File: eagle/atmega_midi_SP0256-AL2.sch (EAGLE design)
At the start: 44 parts, among them U1 6N138, U2 ATMEGA328P_PDIP, U3 SP0256-AL2, U4 TL072P

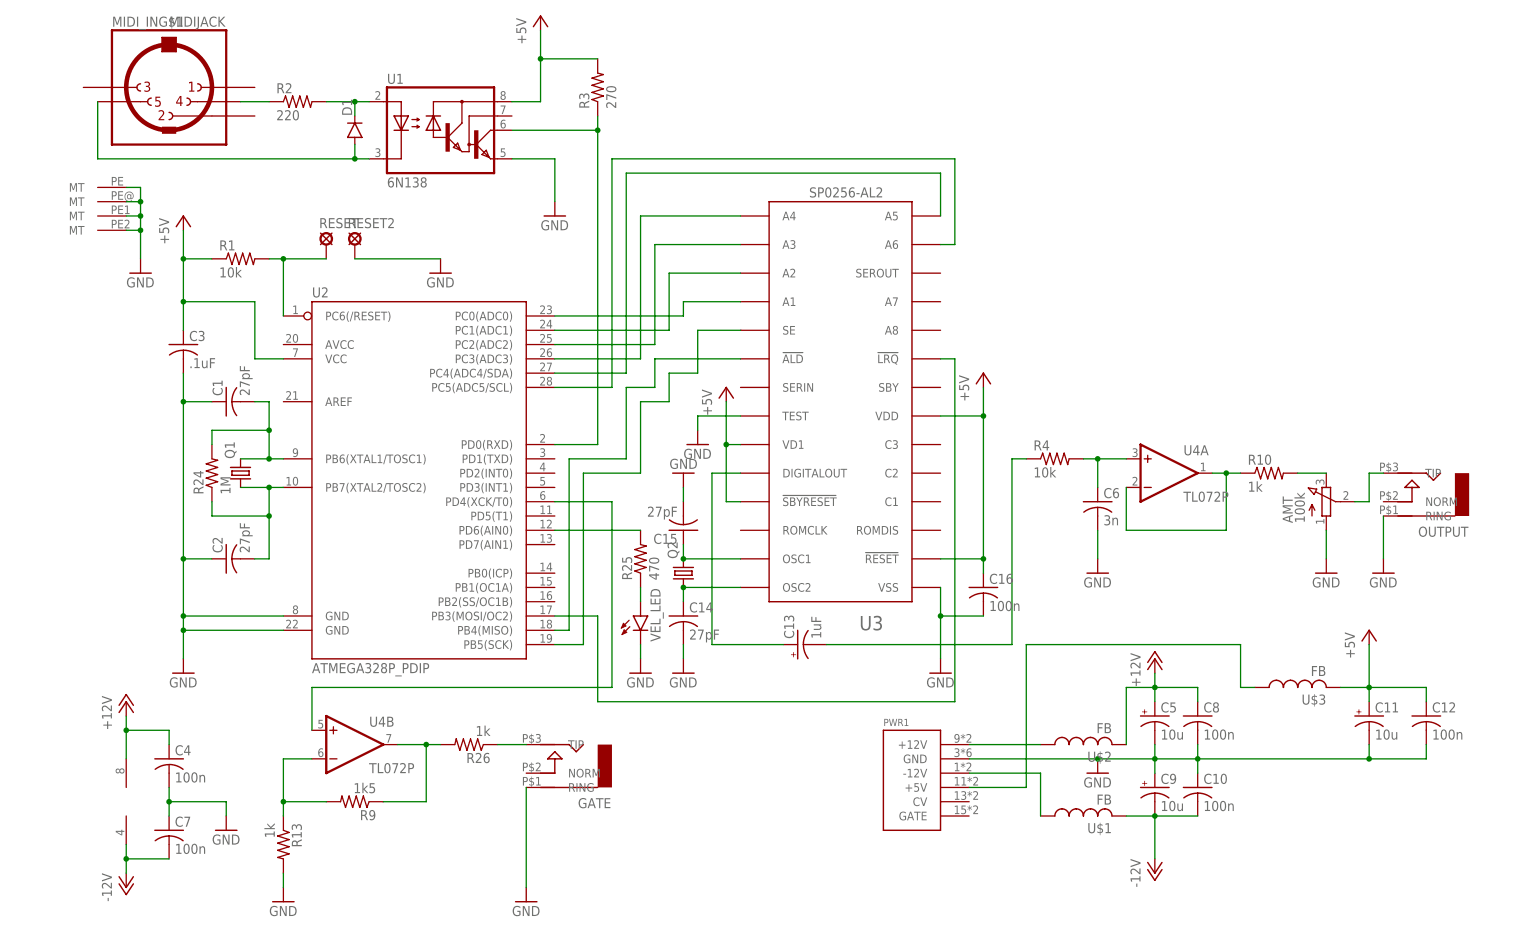
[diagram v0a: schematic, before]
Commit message: schematic corrected for reset control
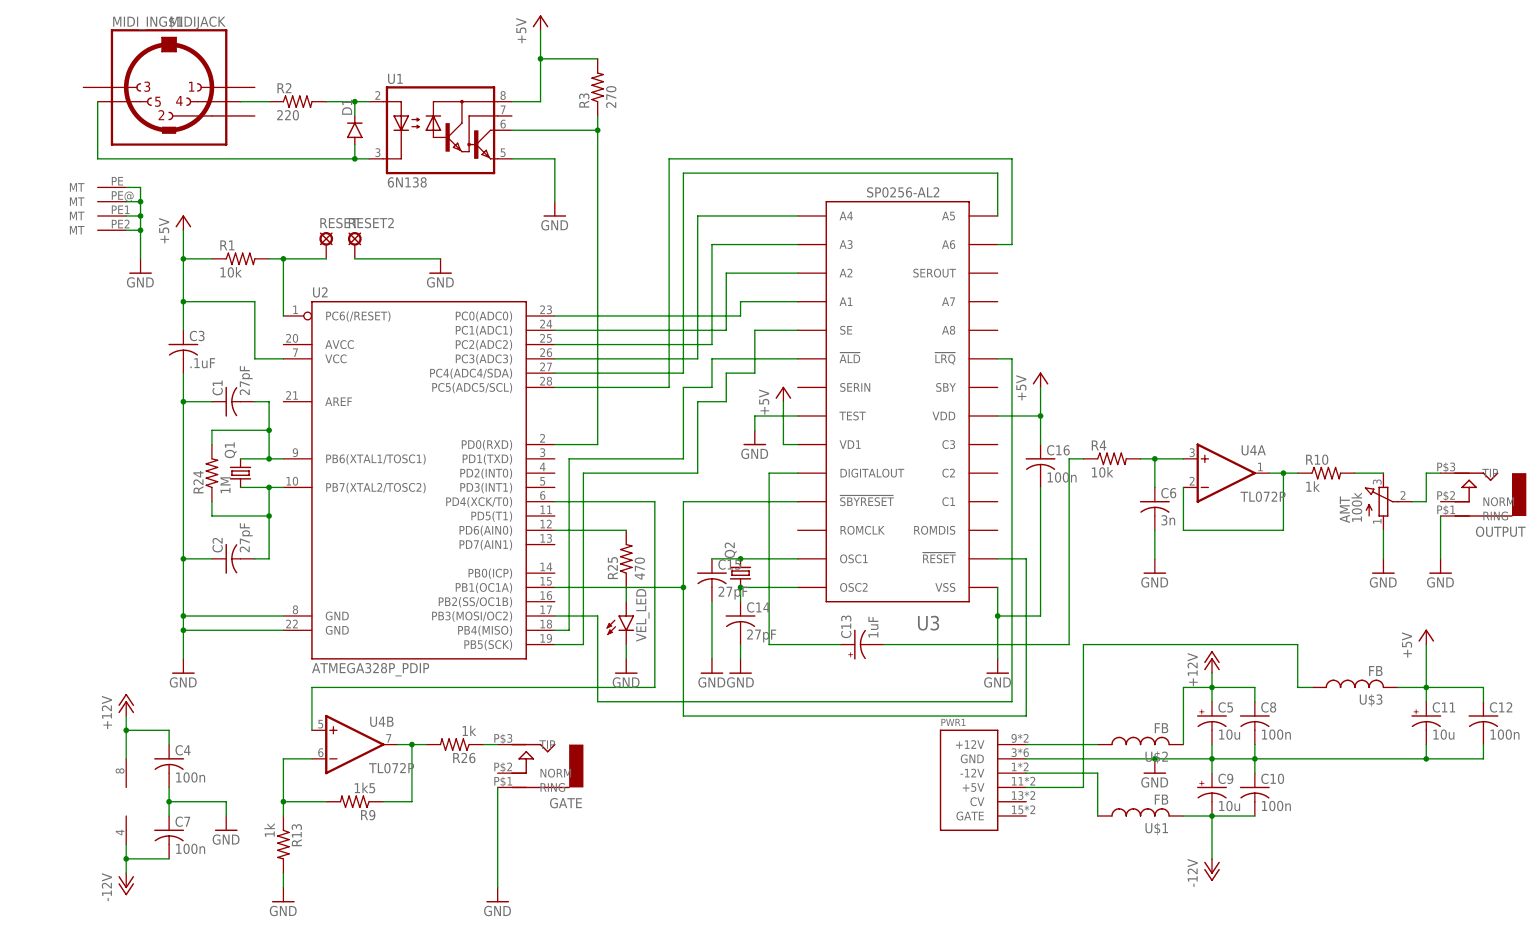
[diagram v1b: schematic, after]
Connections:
- new net N$1: U2.PB1(OC1A), U3.!RESET, U3.!SBYRESET
- net +5V: no longer U3.!RESET, U3.!SBYRESET
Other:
- moved on the sheet: AMT, C10, C11, C12, C13, C14, C15, C16, C5, C6, C8, C9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

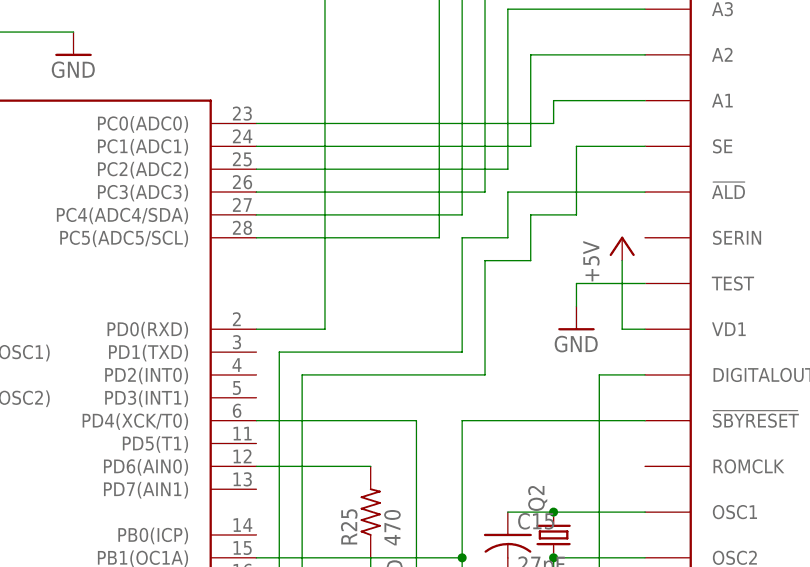
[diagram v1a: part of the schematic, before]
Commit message: board corrected for reset control
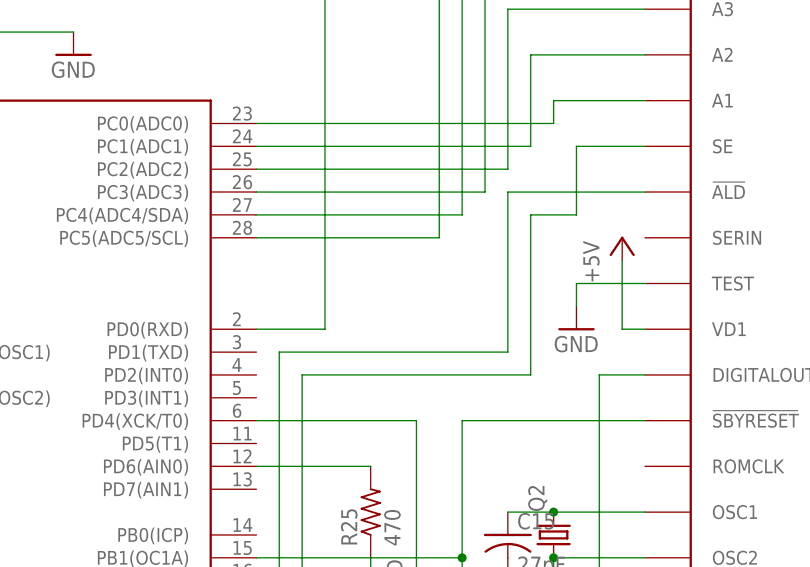
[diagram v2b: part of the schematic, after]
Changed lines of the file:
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@@
 <net name="N$15" class="0">
 <segment>
-<wire x1="68.58" y1="66.04" x2="68.58" y2="60.96" width="0.1524" layer="91"/>
-<wire x1="68.58" y1="60.96" x2="63.5" y2="60.96" width="0.1524" layer="91"/>
-<wire x1="63.5" y1="60.96" x2="63.5" y2="48.26" width="0.1524" layer="91"/>
-<wire x1="63.5" y1="48.26" x2="43.18" y2="48.26" width="0.1524" layer="91"/>
+<wire x1="68.58" y1="66.04" x2="68.58" y2="48.26" width="0.1524" layer="91"/>
+<wire x1="68.58" y1="48.26" x2="43.18" y2="48.26" width="0.1524" layer="91"/>
 <wire x1="43.18" y1="48.26" x2="43.18" y2="17.78" width="0.1524" layer="91"/>
 <pinref part="U2" gate="G$1" pin="PB4(MISO)"/>
@@
 <wire x1="40.64" y1="15.24" x2="45.72" y2="15.24" width="0.1524" layer="91"/>
 <wire x1="45.72" y1="15.24" x2="45.72" y2="45.72" width="0.1524" layer="91"/>
-<wire x1="45.72" y1="45.72" x2="66.04" y2="45.72" width="0.1524" layer="91"/>
-<wire x1="66.04" y1="45.72" x2="66.04" y2="58.42" width="0.1524" layer="91"/>
-<wire x1="66.04" y1="58.42" x2="71.12" y2="58.42" width="0.1524" layer="91"/>
-<wire x1="71.12" y1="58.42" x2="71.12" y2="63.5" width="0.1524" layer="91"/>
+<wire x1="45.72" y1="45.72" x2="71.12" y2="45.72" width="0.1524" layer="91"/>
+<wire x1="71.12" y1="45.72" x2="71.12" y2="63.5" width="0.1524" layer="91"/>
 <wire x1="71.12" y1="63.5" x2="76.2" y2="63.5" width="0.1524" layer="91"/>
 <wire x1="76.2" y1="63.5" x2="76.2" y2="71.12" width="0.1524" layer="91"/>

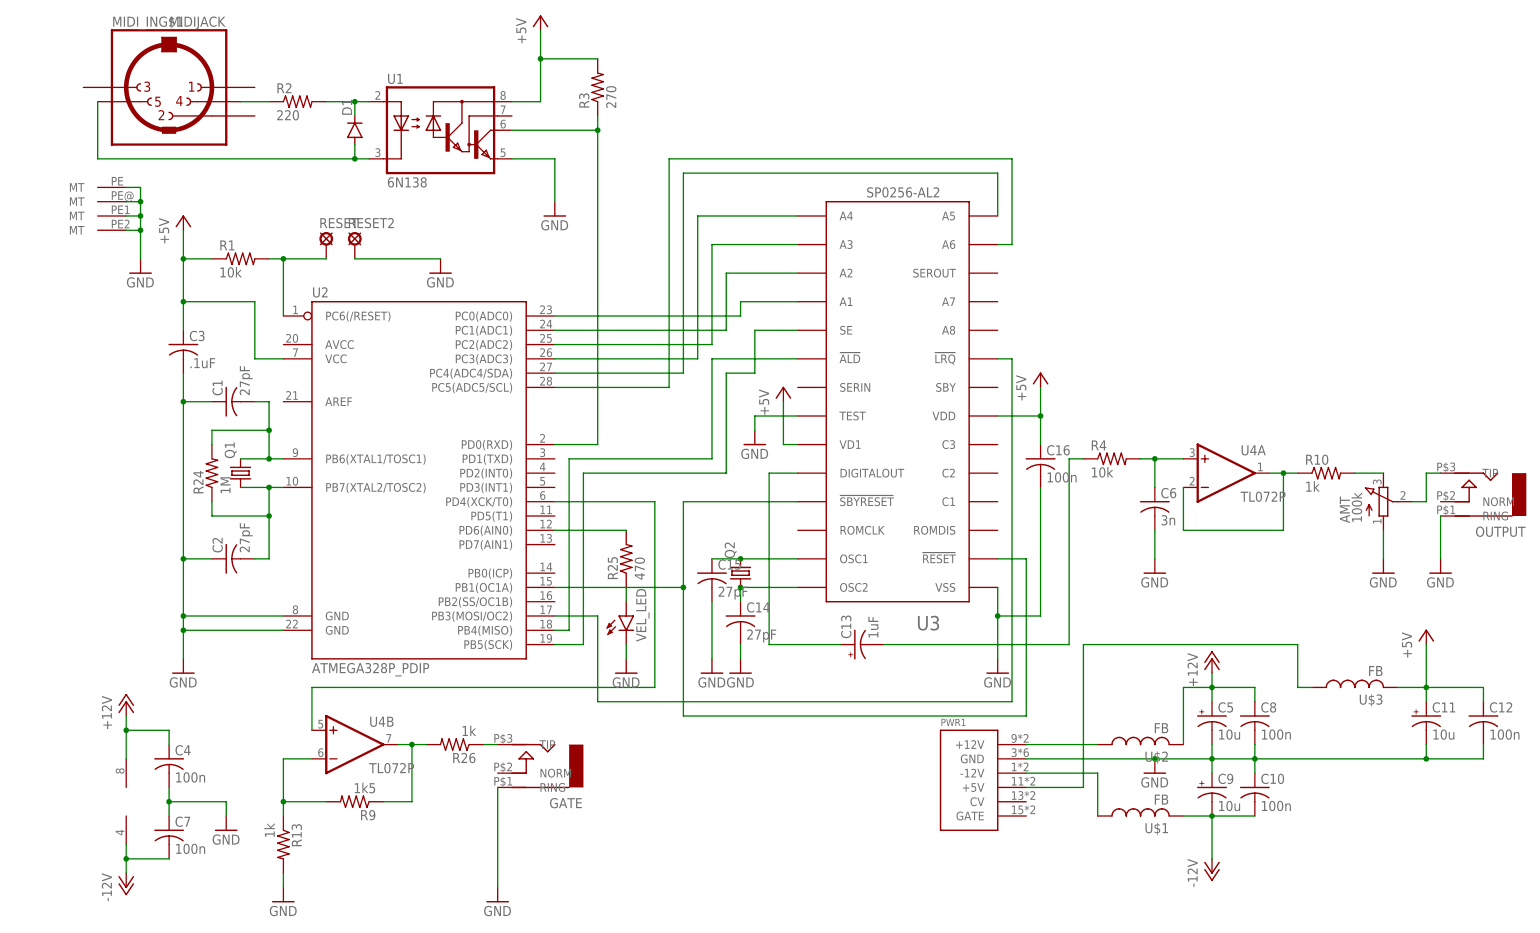
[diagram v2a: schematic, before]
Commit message: added ltc6904
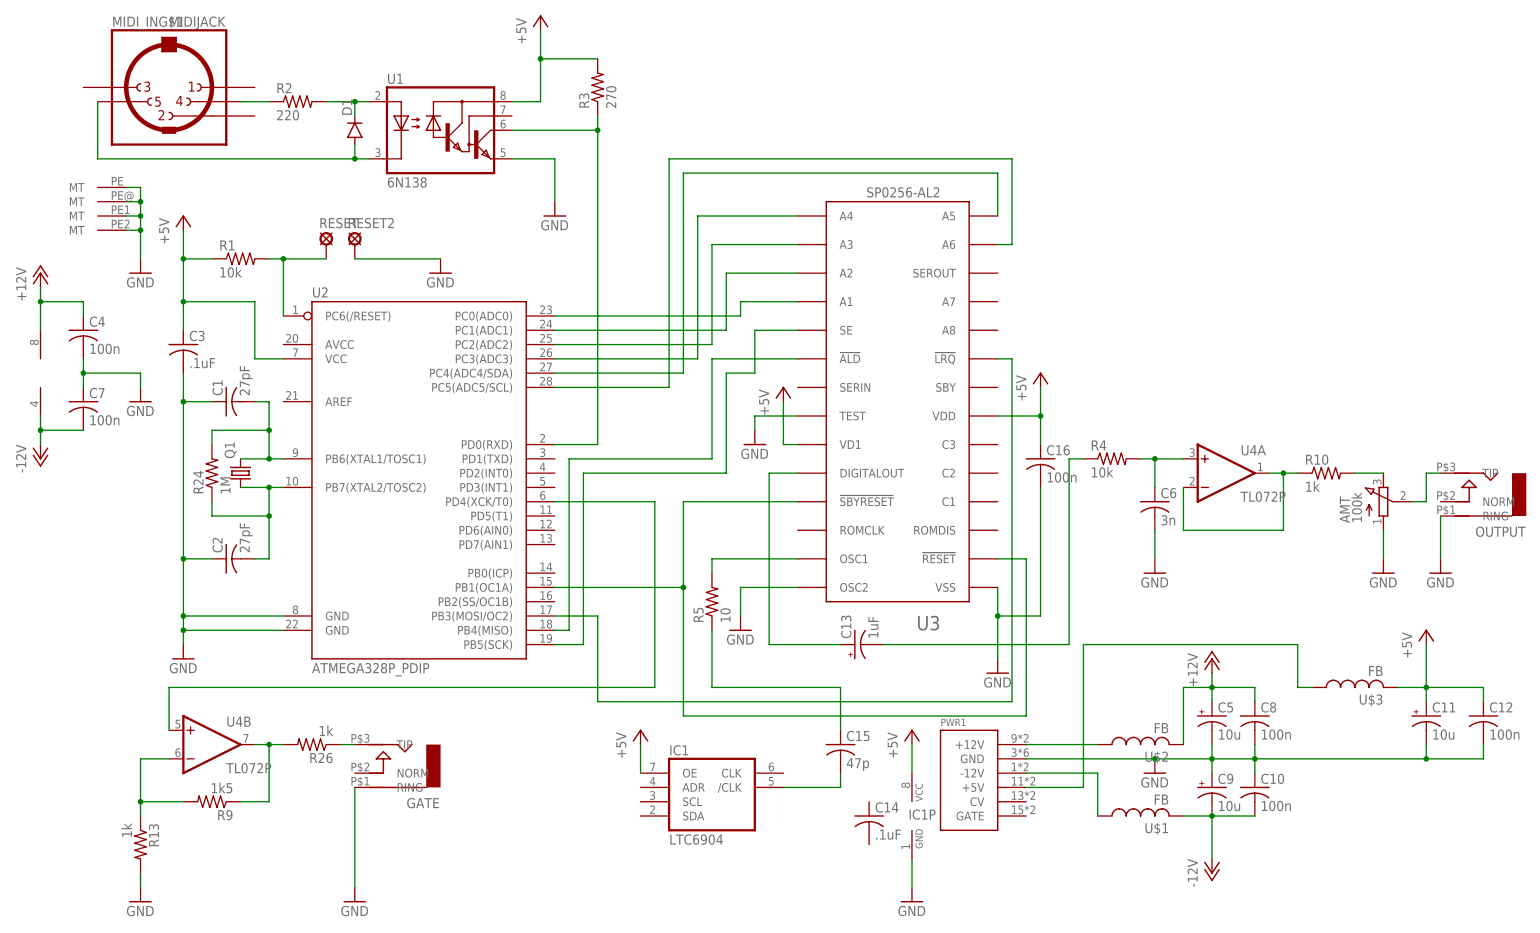
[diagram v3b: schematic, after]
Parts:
- removed Q2: (no value), crystal:CRYSTALHC49S
- removed R25: 470, rcl:R-US_0207/7
- removed VEL_LED: (no value), SparkFun-LED:LED5MM
- added IC1: LTC6904, linear-technology-3:LTC6904
- added R5: 10, rcl:R-US_0207/7
- C14: value 27pF -> .1uF; device rcl:C-US025-040X050 -> rcl:C-US025-030X050
- C15: value 27pF -> 47p; device rcl:C-US025-040X050 -> rcl:C-US050-024X044
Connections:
- removed net N$18: R25.1, VEL_LED.A
- removed net N$20: R25.2, U2.PD6(AIN0)
- removed net N$38: C14.1, Q2.1, U3.OSC2
- new net N$29: C15.2, IC1G$1./CLK
- new net N$33: R5.2, U3.OSC1
- net +5V: now also IC1G$1.OE, IC1P.VCC
- net GND: now also IC1P.GND, U3.OSC2; no longer C14.2, C15.2, VEL_LED.C
- net N$39: now also R5.1; no longer Q2.2, U3.OSC1
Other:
- moved on the sheet: C14, C15, C4, C7, GATE, R13, R26, R9, U4B

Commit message: renamed arduino code file and new board taking shape
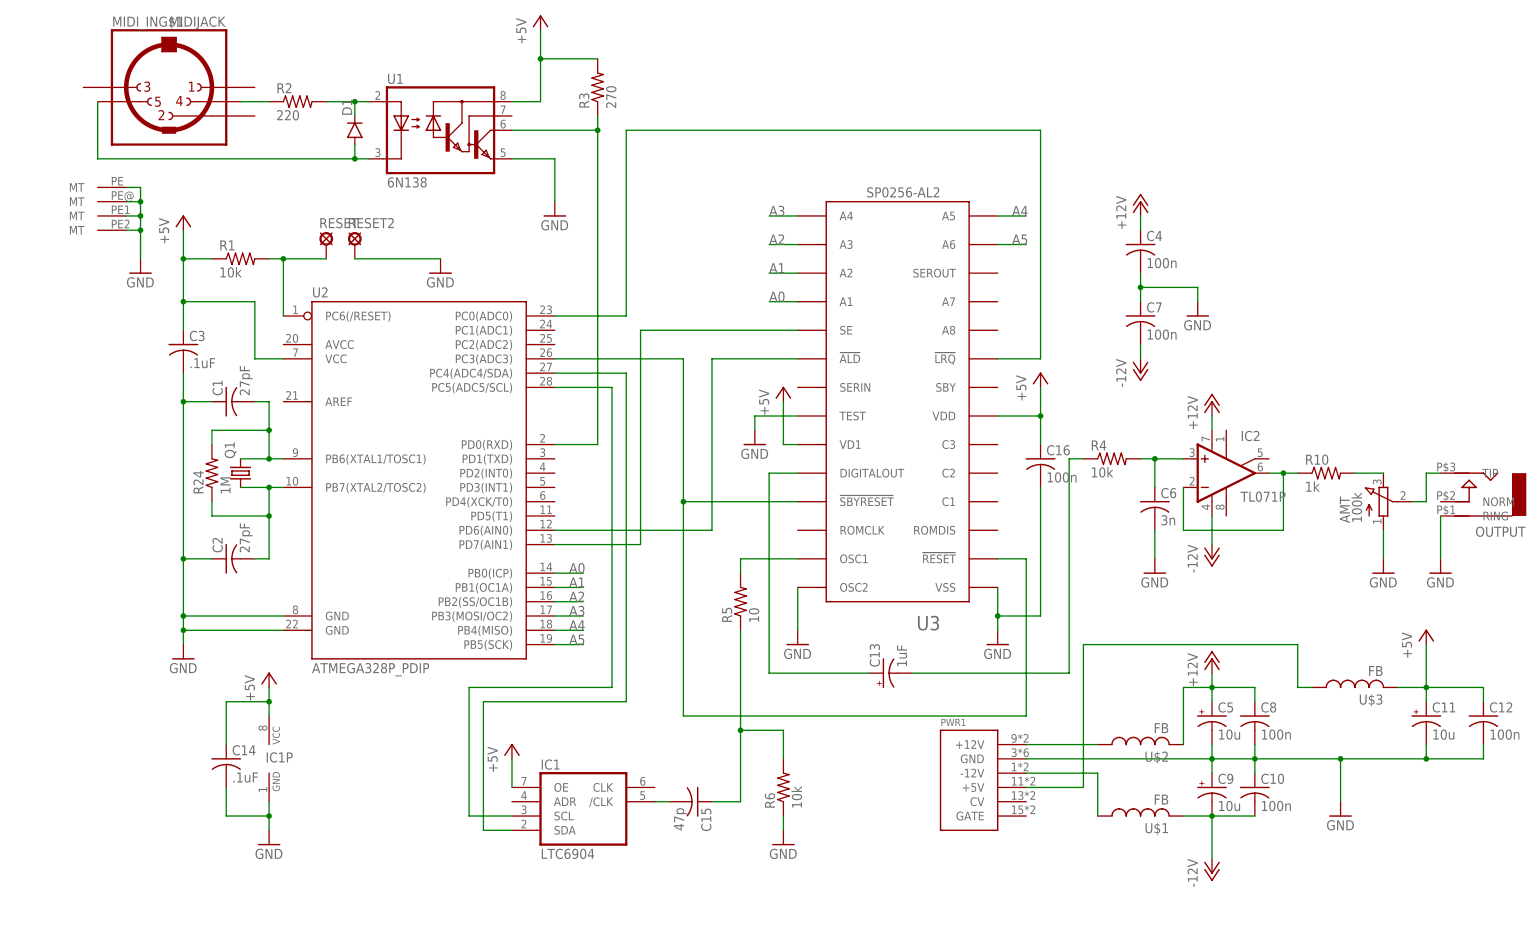
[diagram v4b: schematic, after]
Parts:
- removed GATE: AUDIO-JACK, erthenvar:AUDIO-JACK
- removed R13, R26: 1k, rcl:R-US_0207/7
- removed R9: 1k5, rcl:R-US_0207/7
- removed U4: TL072P, linear:TL072P
- added IC2: TL071P, linear:TL071P
- added R6: 10k, rcl:R-US_0207/7
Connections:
- removed net N$19: U2.PC0(ADC0), U3.A1
- removed net N$21: U2.PC1(ADC1), U3.A2
- removed net N$22: U2.PD4(XCK/T0), U4B.+IN
- removed net N$23: U2.PC2(ADC2), U3.A3
- removed net N$24: U2.PC3(ADC3), U3.A4
- removed net N$25: U2.PC4(ADC4/SDA), U3.A5
- removed net N$26: U2.PC5(ADC5/SCL), U3.A6
- removed net N$27: U2.PB5(SCK), U3.SE
- removed net N$31: GATE.TIP, R26.1
- new net A0: U2.PB0(ICP), U3.A1
- new net A1: U2.PB1(OC1A), U3.A2
- new net A2: U2.PB2(SS/OC1B), U3.A3
- new net A3: U2.PB3(MOSI/OC2), U3.A4
- new net A4: U2.PB4(MISO), U3.A5
- new net A5: U2.PB5(SCK), U3.A6
- new net N$18: IC1G$1.SDA, U2.PC4(ADC4/SDA)
- net +12V: now also IC2.V+; no longer U4P.V+
- net +5V: now also C14.1
- net -12V: now also IC2.V-; no longer U4P.V-
- net GND: now also C14.2, R6.1; no longer GATE.RING, R13.2
- net N$1: now also U2.PC3(ADC3); no longer U2.PB1(OC1A)
- net N$10: now also U2.PD6(AIN0), U3.!ALD; no longer R13.1, R9.2, U4B.-IN
- net N$12: now also IC2.-IN, IC2.OUT; no longer U4A.-IN, U4A.OUT
- net N$15: now also IC1G$1.SCL, U2.PC5(ADC5/SCL); no longer U2.PB4(MISO), U3.!ALD
- net N$16: now also U2.PD7(AIN1), U3.SE; no longer R26.2, R9.1, U4B.OUT
- net N$28: now also U2.PC0(ADC0); no longer U2.PB3(MOSI/OC2)
- net N$39: now also R6.2
- net N$6: now also IC2.+IN; no longer U4A.+IN
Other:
- moved on the sheet: C13, C14, C15, C4, C7, IC1, IC1P, R5
